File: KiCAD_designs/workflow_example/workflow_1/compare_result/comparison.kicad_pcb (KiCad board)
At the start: 2 copper layers, 21 x 18 mm, 5 parts, among them J1 B2B-PH-SM4-TBLFSN, SW1 CUS-12TB, U1 ATTINY45-20SU

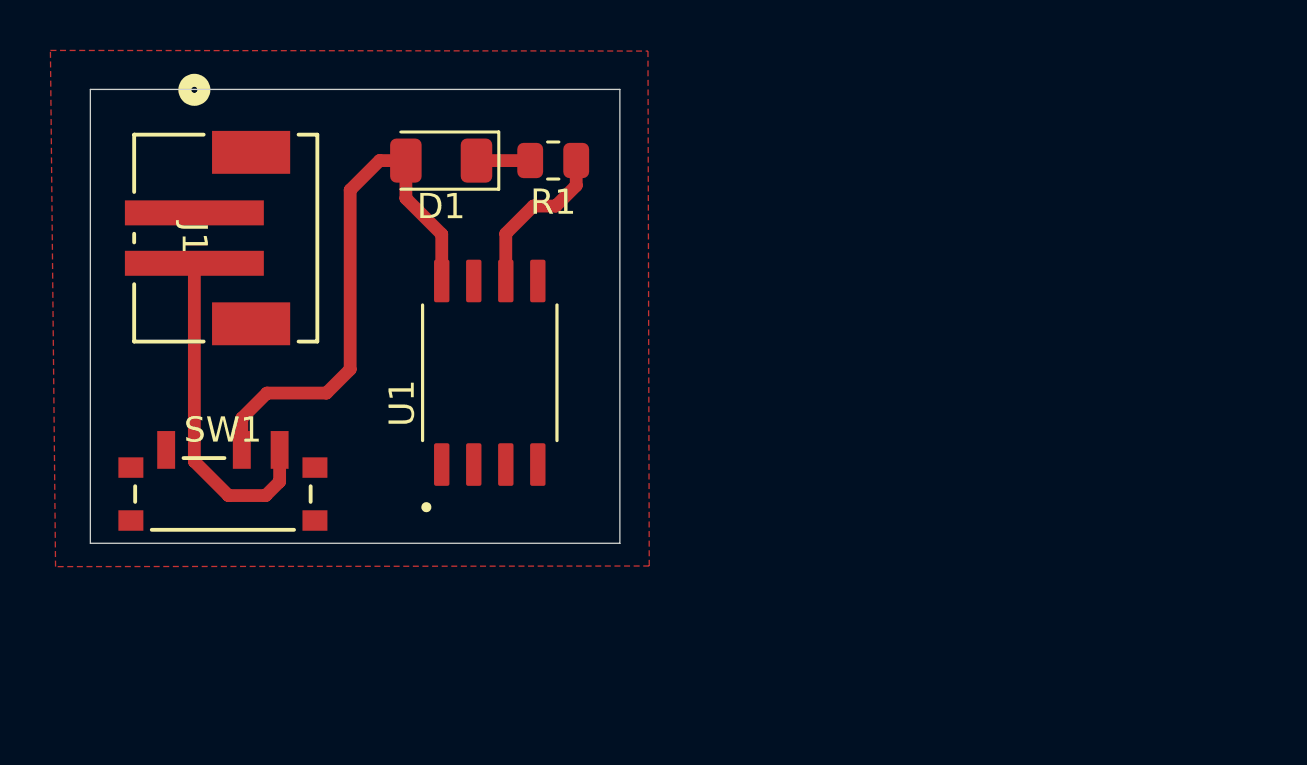
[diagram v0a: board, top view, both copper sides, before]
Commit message: Fixed bug where the edge cuts weren't aligned after comparison
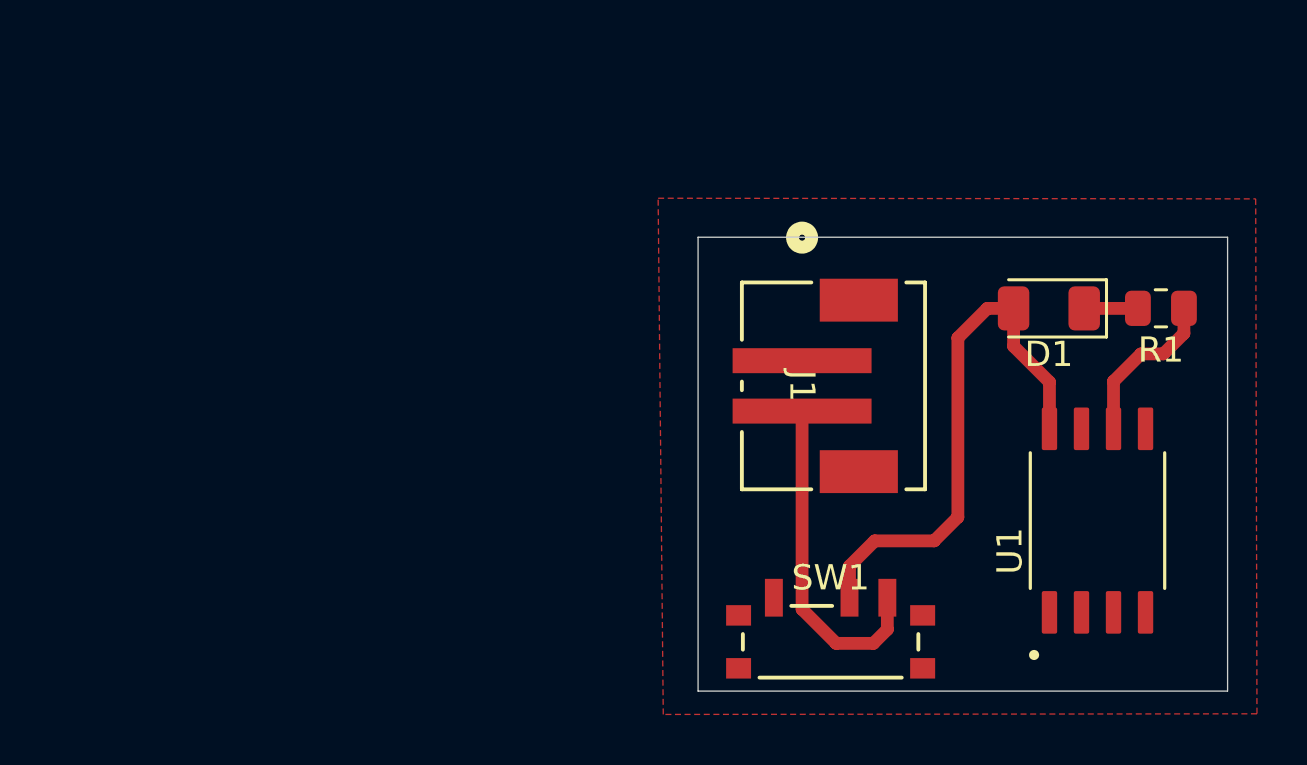
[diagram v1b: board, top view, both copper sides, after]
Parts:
- moved D1 24.8 mm to (120.0, 59.7)
- moved J1 24.8 mm to (111.5, 62.8)
- moved R1 24.8 mm to (124.5, 59.7)
- moved SW1 24.8 mm to (111.4, 72.9)
- moved U1 24.8 mm to (121.9, 68.1)
